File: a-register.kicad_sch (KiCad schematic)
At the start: 22 parts, among them U7 74HCT245, U8 74HCT173, U9 74HCT173

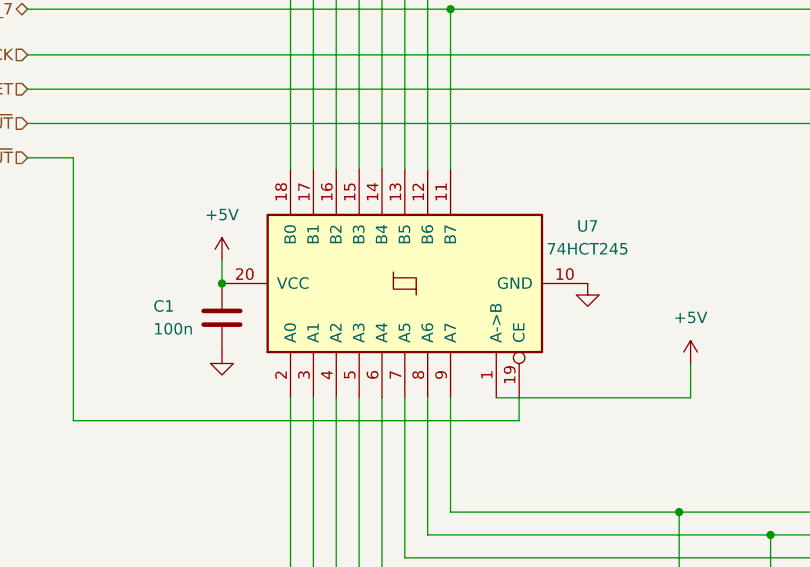
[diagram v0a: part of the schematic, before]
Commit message: changed symbols
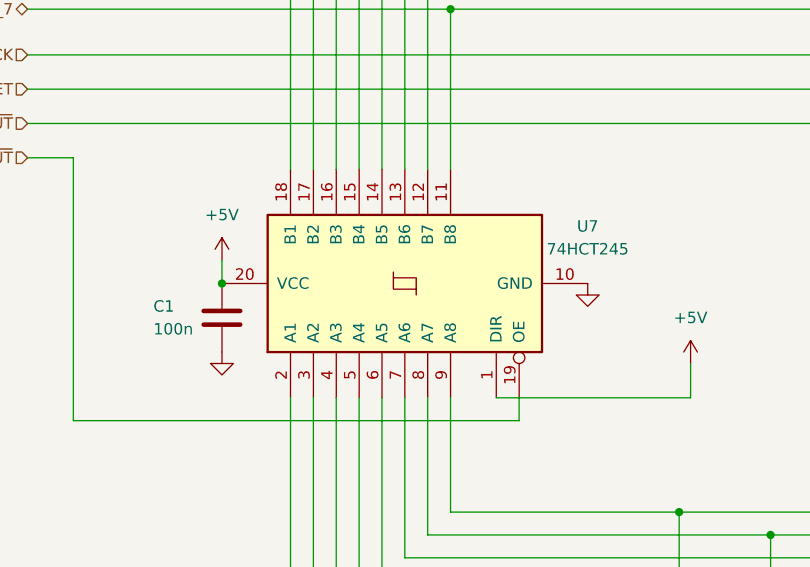
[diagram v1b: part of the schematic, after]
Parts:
- U7: symbol 74xx:74HC245 -> 01_my_library:74HCT245
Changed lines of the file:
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@@
     )
   )
-  (symbol (lib_id "74xx:74HC245") (at 72.39 72.39 90) (unit 1)
+  (symbol (lib_id "01_my_library:74HCT245") (at 72.39 72.39 90) (unit 1)
     (in_bom yes) (on_board yes) (dnp no)
     (property "Reference" "U7" (at 92.71 66.04 90)
@@
       (effects (font (size 1.27 1.27)) hide)
     )
-    (property "Datasheet" "http://www.ti.com/lit/gpn/sn74HC245" (at 72.39 72.39 0)
+    (property "Datasheet" "https://www.ti.com/lit/ds/symlink/sn74hct245.pdf?ts=1702763405638&ref_url=https%253A%252F%252Fwww.google.com%252F" (at 95.25 72.39 0)
       (effects (font (size 1.27 1.27)) hide)
     )

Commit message: cleanup
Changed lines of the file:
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@@
     )
   )
-  (symbol (lib_name "74LS173_1") (lib_id "74xx:74LS173") (at 148.59 72.39 270) (unit 1)
-    (in_bom yes) (on_board yes) (dnp no) (fields_autoplaced)
-    (property "Reference" "U8" (at 171.45 65.4619 90)
-      (effects (font (size 1.27 1.27)))
-    )
-    (property "Value" "74HCT173" (at 171.45 68.0019 90)
+  (symbol (lib_id "74xx:74LS173") (at 148.59 72.39 270) (unit 1)
+    (in_bom yes) (on_board yes) (dnp no) (fields_autoplaced)
+    (property "Reference" "U8" (at 172.72 65.4619 90)
+      (effects (font (size 1.27 1.27)))
+    )
+    (property "Value" "74HCT173" (at 172.72 68.0019 90)
       (effects (font (size 1.27 1.27)))
     )
@@
   (symbol (lib_id "74xx:74LS173") (at 223.52 72.39 270) (unit 1)
     (in_bom yes) (on_board yes) (dnp no) (fields_autoplaced)
-    (property "Reference" "U9" (at 246.38 65.4619 90)
-      (effects (font (size 1.27 1.27)))
-    )
-    (property "Value" "74HCT173" (at 246.38 68.0019 90)
-      (effects (font (size 1.27 1.27)))
-    )
+    (property "Reference" "U9" (at 247.65 65.4619 90)
+      (effects (font (size 1.27 1.27)))
+    )
+    (property "Value" "74HCT173" (at 247.65 68.0019 90)
+      (effects (font (size 1.27 1.27)))
+    )

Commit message: trying to solve issues
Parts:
- added C13: 10n, symbol Device:C
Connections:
- net GND: now also C13.2
- net RESET: now also C13.1
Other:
- note added: "In order to make the A register not reset randomly I had to add a 10n capacitor to ground. Do not know why. This might be a breadboard thing."

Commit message: regenerated BOM
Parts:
- C13: footprint (none) -> 01_my_library:C_Disc_D4.0mm_W2.6mm_P2.50mm
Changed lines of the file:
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@@
       (effects (font (size 1.27 1.27)) (justify left))
     )
-    (property "Footprint" "" (at 221.9452 46.99 0)
+    (property "Footprint" "01_my_library:C_Disc_D4.0mm_W2.6mm_P2.50mm" (at 221.9452 46.99 0)
       (effects (font (size 1.27 1.27)) hide)
     )

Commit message: kicad update
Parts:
- D13, D14, D15, D16, D17, D18, D19, D20: footprint LED_THT:LED_D5.0mm -> 01_my_library:LED_D5.0mm
- renumbered C1 to C14, C1 to C15, C1 to C16
